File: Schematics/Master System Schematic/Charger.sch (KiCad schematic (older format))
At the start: 9 parts, among them J7 WallSocket, K6 Safety Relay, U5 TSM2500

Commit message: Annotations
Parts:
- gave numbers to parts that had none: 3
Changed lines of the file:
@@
 AR Path="/61EEF404" Ref="K?"  Part="1"
 AR Path="/61ECC7CF/61EEF404" Ref="K6"  Part="1"
-F 0 "K?" H 3850 2233 50  0000 C CNN
+F 0 "K6" H 3850 2233 50  0000 C CNN
 F 1 "Safety Relay" H 3850 2324 50  0000 C CNN
 F 2 "Relay_THT:Relay_DPST_Fujitsu_FTR-F1A" H 3850 2350 50  0001 C CNN
@@
 AR Path="/61EEF40A" Ref="F?"  Part="1"
 AR Path="/61ECC7CF/61EEF40A" Ref="F1"  Part="1"
-F 0 "F?" V 6000 2950 50  0000 C CNN
+F 0 "F1" V 6000 2950 50  0000 C CNN
 F 1 "10A" V 5800 2950 50  0000 C CNN
 F 2 "" V 5830 2950 50  0001 C CNN
@@
 AR Path="/61EEF410" Ref="U?"  Part="1"
 AR Path="/61ECC7CF/61EEF410" Ref="U5"  Part="1"
-F 0 "U?" H 5550 4350 50  0001 C CNN
+F 0 "U5" H 5550 4350 50  0001 C CNN
 F 1 "TSM2500" H 5600 4383 50  0000 C CNN
 F 2 "" H 5550 4350 50  0001 C CNN
@@
 AR Path="/61EEF417" Ref="F?"  Part="1"
 AR Path="/61ECC7CF/61EEF417" Ref="F4"  Part="1"
-F 0 "F?" V 6253 4200 50  0000 C CNN
+F 0 "F4" V 6253 4200 50  0000 C CNN
 F 1 "20A" V 6344 4200 50  0000 C CNN
 F 2 "" V 6380 4200 50  0001 C CNN
@@
 AR Path="/61EEF421" Ref="J?"  Part="1"
 AR Path="/61ECC7CF/61EEF421" Ref="J7"  Part="1"
-F 0 "J?" H 6506 2454 50  0000 C CNN
+F 0 "J7" H 6506 2454 50  0000 C CNN
 F 1 "WallSocket" H 6506 2545 50  0000 C CNN
 F 2 "" H 6200 3050 50  0001 C CNN
@@
 CAN_H
 $Comp
-L Converter_ACDC:HLK-PM12 PS?
+L Converter_ACDC:HLK-PM12 PS1
 U 1 1 6015DD85
 P 5500 2100
-F 0 "PS?" H 5500 1783 50  0000 C CNN
+F 0 "PS1" H 5500 1783 50  0000 C CNN
 F 1 "PLACEHOLDER" H 5500 1874 50  0000 C CNN
 F 2 "Converter_ACDC:Converter_ACDC_HiLink_HLK-PMxx" H 5500 1800 50  0001 C CNN
@@
 	6100 2950 6050 2950
 $Comp
-L Device:Fuse F?
+L Device:Fuse F86
 U 1 1 6016ADF1
 P 6100 2200
-F 0 "F?" H 6160 2246 50  0000 L CNN
+F 0 "F86" H 6160 2246 50  0000 L CNN
 F 1 "Fuse" H 6160 2155 50  0000 L CNN
 F 2 "" V 6030 2200 50  0001 C CNN
@@
 AR Path="/6017BDE1" Ref="F?"  Part="1"
 AR Path="/61ECC7CF/6017BDE1" Ref="F3"  Part="1"
-F 0 "F?" V 6253 4050 50  0000 C CNN
+F 0 "F3" V 6253 4050 50  0000 C CNN
 F 1 "20A" V 6344 4050 50  0000 C CNN
 F 2 "" V 6380 4050 50  0001 C CNN
@@
 	6800 5450 6800 4050
 $Comp
-L Device:Fuse F?
+L Device:Fuse F2
 U 1 1 5FA10442
 P 4650 2200
-F 0 "F?" V 4847 2200 50  0000 C CNN
+F 0 "F2" V 4847 2200 50  0000 C CNN
 F 1 "Fuse" V 4756 2200 50  0000 C CNN
 F 2 "" V 4580 2200 50  0001 C CNN

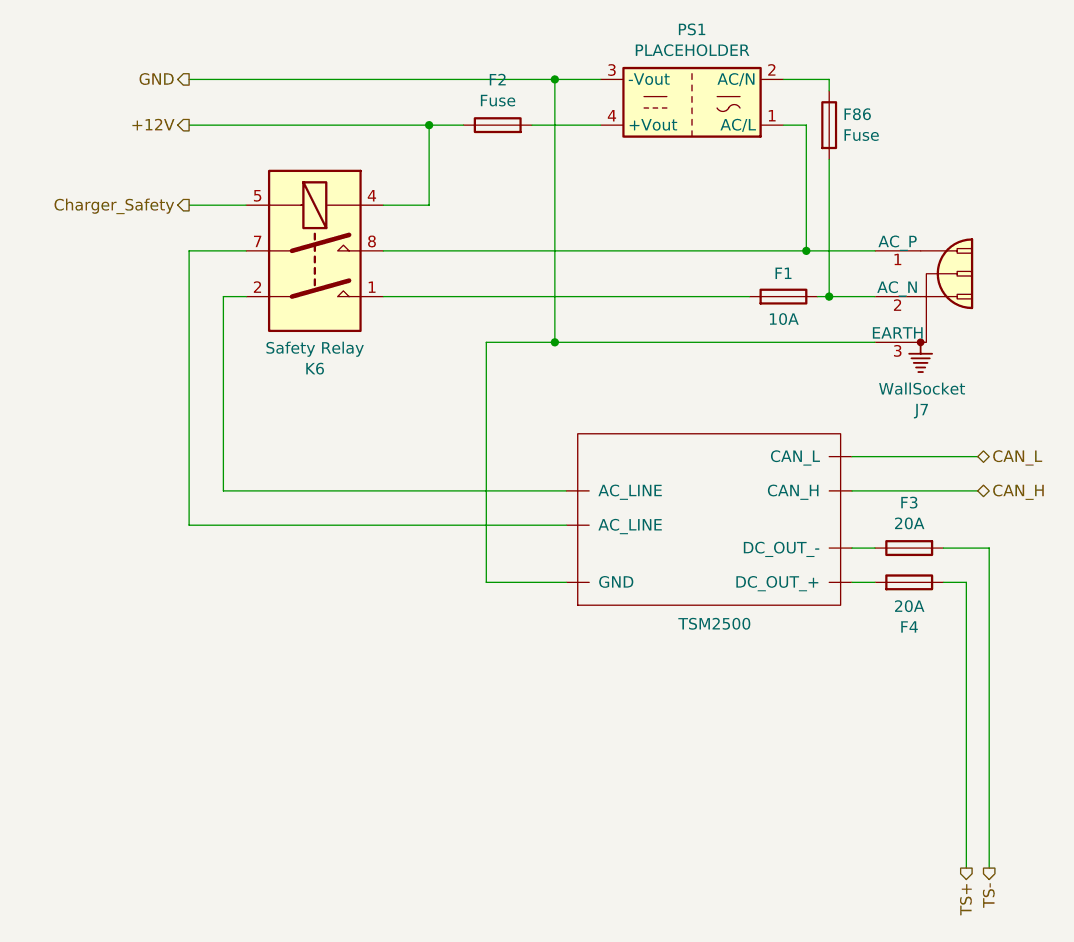
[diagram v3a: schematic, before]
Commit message: Charging Schematic Updates
Added Shielding, added fuses, rearanged F1, removed 2 pin connector.
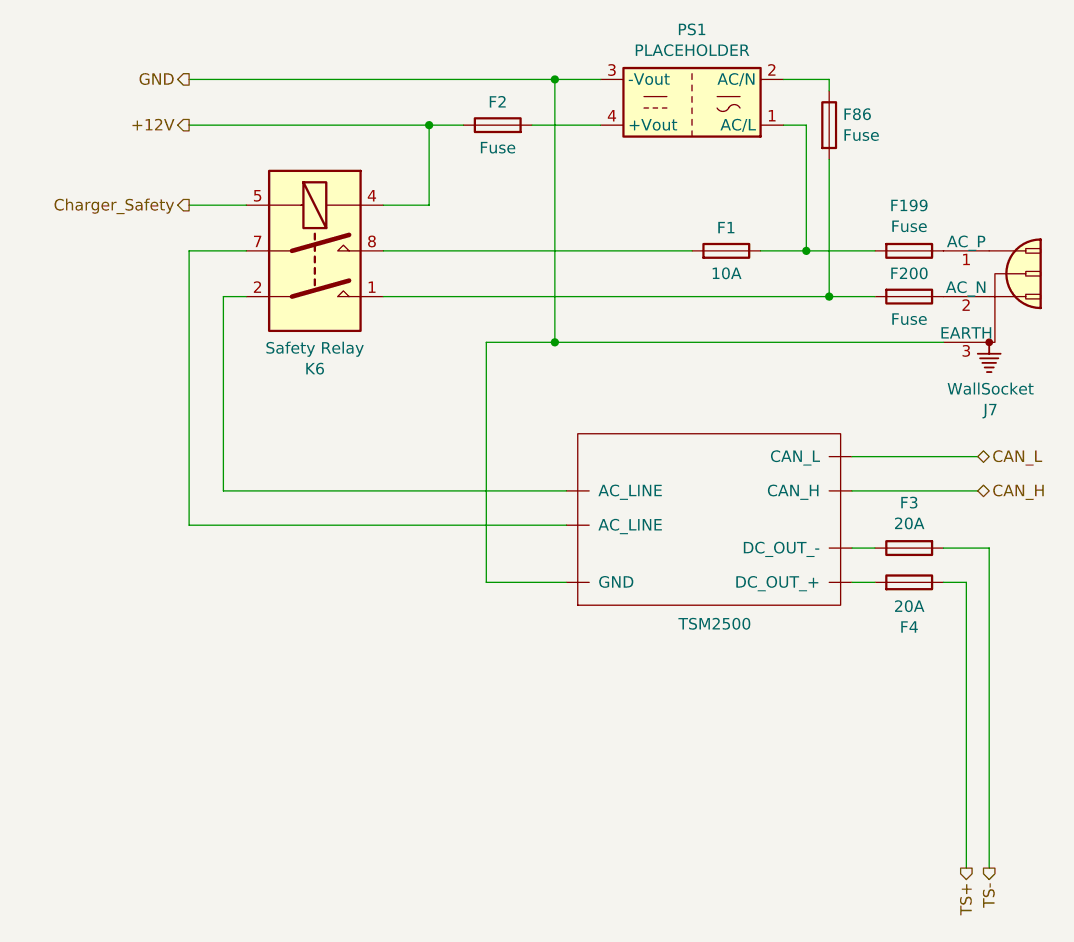
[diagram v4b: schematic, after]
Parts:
- added F199, F200: Fuse, symbol Device:Fuse
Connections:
- net at K6.1: now also F86.2, F200.2; no longer F1.2
- new net: F1.1, F199.2, PS1.1 (AC/L)
- new net: F199.1, J7.1 (AC_P)
- new net: F200.1, J7.2 (AC_N)
- new net: F1.2, K6.8
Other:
- moved on the sheet: F1, J7
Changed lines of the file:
@@
 L Device:Fuse F?
 U 1 1 61EEF40A
-P 5900 2950
+P 5650 2750
 AR Path="/61EEF40A" Ref="F?"  Part="1"
 AR Path="/61ECC7CF/61EEF40A" Ref="F1"  Part="1"
-F 0 "F1" V 6000 2950 50  0000 C CNN
-F 1 "10A" V 5800 2950 50  0000 C CNN
-F 2 "" V 5830 2950 50  0001 C CNN
-F 3 "~" H 5900 2950 50  0001 C CNN
-	1    5900 2950
+F 0 "F1" V 5750 2750 50  0000 C CNN
+F 1 "10A" V 5550 2750 50  0000 C CNN
+F 2 "" V 5580 2750 50  0001 C CNN
+F 3 "~" H 5650 2750 50  0001 C CNN
+	1    5650 2750
 	0    1    -1   0
 $EndComp
@@
 L Connector:Conn_WallSocket_Earth J?
 U 1 1 61EEF421
-P 6500 2950
+P 6800 2950
 AR Path="/61EEF421" Ref="J?"  Part="1"
 AR Path="/61ECC7CF/61EEF421" Ref="J7"  Part="1"
-F 0 "J7" H 6506 2454 50  0000 C CNN
-F 1 "WallSocket" H 6506 2545 50  0000 C CNN
-F 2 "" H 6200 3050 50  0001 C CNN
-F 3 "~" H 6200 3050 50  0001 C CNN
-	1    6500 2950
+F 0 "J7" H 6806 2454 50  0000 C CNN
+F 1 "WallSocket" H 6806 2545 50  0000 C CNN
+F 2 "" H 6500 3050 50  0001 C CNN
+F 3 "~" H 6500 3050 50  0001 C CNN
+	1    6800 2950
 	1    0    0    -1
 $EndComp
@@
 	6100 2350 6100 2950
 Connection ~ 6100 2950
-Wire Wire Line
-	6100 2950 6050 2950
 $Comp
 L Device:Fuse F86
@@
 Wire Wire Line
 	6000 2200 6000 2750
-Connection ~ 6000 2750
 Wire Wire Line
 	6000 2750 6300 2750
@@
 Wire Wire Line
 	4900 3150 4600 3150
-Wire Wire Line
-	4900 3150 6300 3150
 Wire Wire Line
 	4600 3150 4600 4200
@@
 U 1 1 5FA10442
 P 4650 2200
-F 0 "F2" V 4847 2200 50  0000 C CNN
-F 1 "Fuse" V 4756 2200 50  0000 C CNN
+F 0 "F2" V 4750 2200 50  0000 C CNN
+F 1 "Fuse" V 4550 2200 50  0000 C CNN
 F 2 "" V 4580 2200 50  0001 C CNN
 F 3 "~" H 4650 2200 50  0001 C CNN
@@
 	4800 2200 5100 2200
 Wire Wire Line
-	4150 2750 6000 2750
-Wire Wire Line
 	4500 2200 4350 2200
 Wire Wire Line
@@
 Wire Wire Line
 	4350 2550 4150 2550
-Wire Wire Line
-	4150 2950 5750 2950
 Wire Wire Line
 	3450 3800 4950 3800
@@
 	3300 2200 4350 2200
 Connection ~ 4350 2200
+Wire Wire Line
+	4150 2750 5500 2750
+Wire Wire Line
+	5800 2750 6000 2750
+Connection ~ 6000 2750
+Wire Wire Line
+	4150 2950 6100 2950
+$Comp
+L Device:Fuse F200
+U 1 1 603DFD27
+P 6450 2950
+F 0 "F200" V 6350 2950 50  0000 C CNN
+F 1 "Fuse" V 6550 2950 50  0000 C CNN
+F 2 "" V 6380 2950 50  0001 C CNN
+F 3 "~" H 6450 2950 50  0001 C CNN
+	1    6450 2950
+	0    1    1    0
+$EndComp
+$Comp
+L Device:Fuse F199
+U 1 1 603DB64B
+P 6450 2750
+F 0 "F199" V 6253 2750 50  0000 C CNN
+F 1 "Fuse" V 6344 2750 50  0000 C CNN
+F 2 "" V 6380 2750 50  0001 C CNN
+F 3 "~" H 6450 2750 50  0001 C CNN
+	1    6450 2750
+	0    1    1    0
+$EndComp
+Wire Wire Line
+	4900 3150 6600 3150
 $EndSCHEMATC

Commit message: Fixed mistakes
Deleted unneeded shielding line and neutral fuse line
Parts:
- removed F200: Fuse, symbol Device:Fuse
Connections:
- net at F86.2, K6.1: now also J7.2 (AC_N)
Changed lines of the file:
@@
 	0    1    -1   0
 $EndComp
-Wire Wire Line
-	6300 2950 6100 2950
 $Comp
 L Connector:Conn_WallSocket_Earth J?
@@
 	4150 2950 6100 2950
 $Comp
-L Device:Fuse F200
-U 1 1 603DFD27
-P 6450 2950
-F 0 "F200" V 6350 2950 50  0000 C CNN
-F 1 "Fuse" V 6550 2950 50  0000 C CNN
-F 2 "" V 6380 2950 50  0001 C CNN
-F 3 "~" H 6450 2950 50  0001 C CNN
-	1    6450 2950
-	0    1    1    0
-$EndComp
-$Comp
 L Device:Fuse F199
 U 1 1 603DB64B
@@
 Wire Wire Line
 	4900 3150 6600 3150
+Wire Wire Line
+	6100 2950 6600 2950
 $EndSCHEMATC

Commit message: Moved F86 to Positive line
Another quick fix moving F86 to Positive line from neutral
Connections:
- net at F1.1, F199.2: now also F86.2; no longer PS1.1 (AC/L)
- net at F86.1: now also PS1.1 (AC/L); no longer PS1.2 (AC/N)
- net at J7.2 (AC_N), K6.1: now also PS1.2 (AC/N); no longer F86.2
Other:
- moved on the sheet: F86
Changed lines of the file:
@@
 Wire Wire Line
 	5900 2000 6100 2000
-Wire Wire Line
-	6100 2350 6100 2950
 Connection ~ 6100 2950
-$Comp
-L Device:Fuse F86
-U 1 1 6016ADF1
-P 6100 2200
-F 0 "F86" H 6160 2246 50  0000 L CNN
-F 1 "Fuse" H 6160 2155 50  0000 L CNN
-F 2 "" V 6030 2200 50  0001 C CNN
-F 3 "~" H 6100 2200 50  0001 C CNN
-	1    6100 2200
-	1    0    0    -1
-$EndComp
-Wire Wire Line
-	6100 2050 6100 2000
-Wire Wire Line
-	6000 2200 6000 2750
-Wire Wire Line
-	6000 2750 6300 2750
 Wire Wire Line
 	5100 2000 4900 2000
@@
 	4150 2750 5500 2750
 Wire Wire Line
-	5800 2750 6000 2750
-Connection ~ 6000 2750
-Wire Wire Line
 	4150 2950 6100 2950
 $Comp
@@
 Wire Wire Line
 	6100 2950 6600 2950
+$Comp
+L Device:Fuse F86
+U 1 1 6016ADF1
+P 6000 2350
+F 0 "F86" H 5750 2350 50  0000 L CNN
+F 1 "Fuse" H 5750 2250 50  0000 L CNN
+F 2 "" V 5930 2350 50  0001 C CNN
+F 3 "~" H 6000 2350 50  0001 C CNN
+	1    6000 2350
+	1    0    0    -1
+$EndComp
+Wire Wire Line
+	5800 2750 6000 2750
+Wire Wire Line
+	6000 2500 6000 2750
+Connection ~ 6000 2750
+Wire Wire Line
+	6000 2750 6300 2750
+Wire Wire Line
+	6100 2000 6100 2950
 $EndSCHEMATC

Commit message: Edited Fuse Values
Edited Fuse Values
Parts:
- F1: value 10A -> 15A
- F199, F86: value Fuse -> 15A
- F2: value Fuse -> 10A
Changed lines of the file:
@@
 AR Path="/61ECC7CF/61EEF40A" Ref="F1"  Part="1"
 F 0 "F1" V 5750 2750 50  0000 C CNN
-F 1 "10A" V 5550 2750 50  0000 C CNN
+F 1 "15A" V 5550 2750 50  0000 C CNN
 F 2 "" V 5580 2750 50  0001 C CNN
 F 3 "~" H 5650 2750 50  0001 C CNN
@@
 P 4650 2200
 F 0 "F2" V 4750 2200 50  0000 C CNN
-F 1 "Fuse" V 4550 2200 50  0000 C CNN
+F 1 "10A" V 4550 2200 50  0000 C CNN
 F 2 "" V 4580 2200 50  0001 C CNN
 F 3 "~" H 4650 2200 50  0001 C CNN
@@
 P 6450 2750
 F 0 "F199" V 6253 2750 50  0000 C CNN
-F 1 "Fuse" V 6344 2750 50  0000 C CNN
+F 1 "15A" V 6344 2750 50  0000 C CNN
 F 2 "" V 6380 2750 50  0001 C CNN
 F 3 "~" H 6450 2750 50  0001 C CNN
@@
 P 6000 2350
 F 0 "F86" H 5750 2350 50  0000 L CNN
-F 1 "Fuse" H 5750 2250 50  0000 L CNN
+F 1 "15A" H 5750 2250 50  0000 L CNN
 F 2 "" V 5930 2350 50  0001 C CNN
 F 3 "~" H 6000 2350 50  0001 C CNN

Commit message: F86 Update
Updated Fuse F86
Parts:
- F86: value 15A -> 1A
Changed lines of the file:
@@
 Wire Wire Line
 	6600 4050 6800 4050
-Wire Wire Line
-	6800 5450 6800 4050
 $Comp
 L Device:Fuse F2
@@
 P 6000 2350
 F 0 "F86" H 5750 2350 50  0000 L CNN
-F 1 "15A" H 5750 2250 50  0000 L CNN
+F 1 "1A" H 5750 2250 50  0000 L CNN
 F 2 "" V 5930 2350 50  0001 C CNN
 F 3 "~" H 6000 2350 50  0001 C CNN
@@
 Wire Wire Line
 	6100 2000 6100 2950
+Wire Wire Line
+	6800 5450 6800 4050
+Text Label 6700 4700 3    50   ~ 0
+W1_2WG
 $EndSCHEMATC
